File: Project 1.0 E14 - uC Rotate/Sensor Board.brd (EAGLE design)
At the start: 40 x 75 mm, 95 parts, among them IC1 LT1963EST-1.5, IC2 LT1963EST-1.5, IC4 LT1963EST-1.5

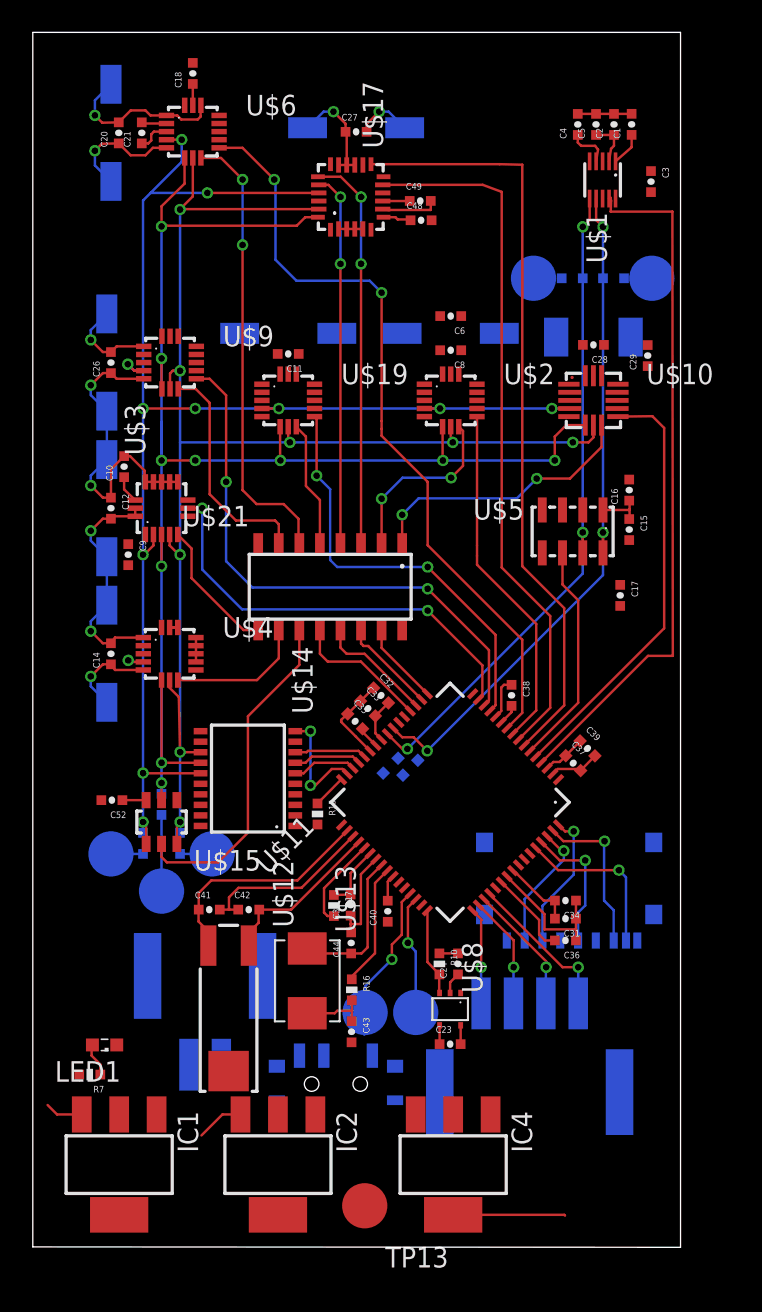
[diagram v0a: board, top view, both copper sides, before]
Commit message: Sensor test board: All traces have been confirmed connected except for power and GND. The issues from previous commit remain to be addresed.
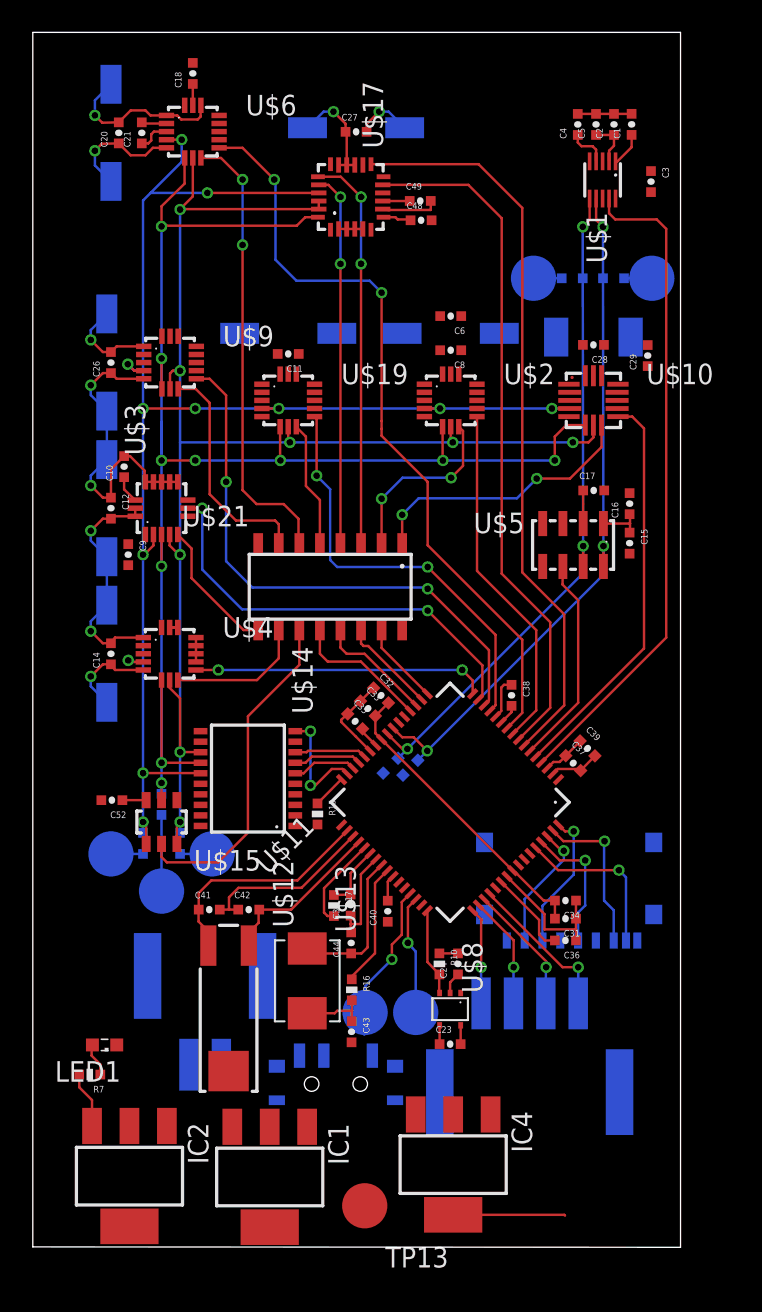
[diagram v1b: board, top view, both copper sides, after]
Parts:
- moved IC1 9.33 mm to (14.6, 4.32)
- moved IC2 9.20 mm to (5.97, 4.37)
- moved C17 6.68 mm to (34.6, 46.7), turned to 0 degrees
- moved C15 0.84 mm to (36.9, 43.5)
- moved C16 0.84 mm to (36.9, 45.9)
- moved U$5 0.84 mm to (33.4, 43.3)
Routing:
- net INT2-LPS331: track 0.00 -> 18.2 mm, vias 0 -> 2
- net 1.2V: track 7.31 -> 18.8 mm
- net 3.0V: track 2.35 -> 0.00 mm
- net INT1-MAG3110: track 43.1 -> 41.0 mm
- net N$5: track 0.00 -> 2.04 mm
- net INT2-ADXL362: track 26.7 -> 25.0 mm
- net N$26: track 0.00 -> 1.74 mm
- net N$24: track 0.00 -> 1.72 mm
- net LSM9D-INT1-XM: track 47.3 -> 45.7 mm
- net MISO-B: track 89.4 -> 90.8 mm
- net LSM9D-INT-G: track 43.3 -> 42.4 mm
- net INT1-MPL311: track 13.9 -> 13.0 mm
- net SDA-0: track 41.5 -> 42.4 mm
- net SCL-0: track 42.7 -> 43.6 mm
- net MOSI-B: track 96.0 -> 96.7 mm

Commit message: Sensor Test Board: Corrected LSM9D0 interrupt issue by adding int2-XM and removing int1_G and replacing it with DRDY_G. Some 3.3v traces have been connected but these wil need to be checked to ensure the LDO is not overloaded.
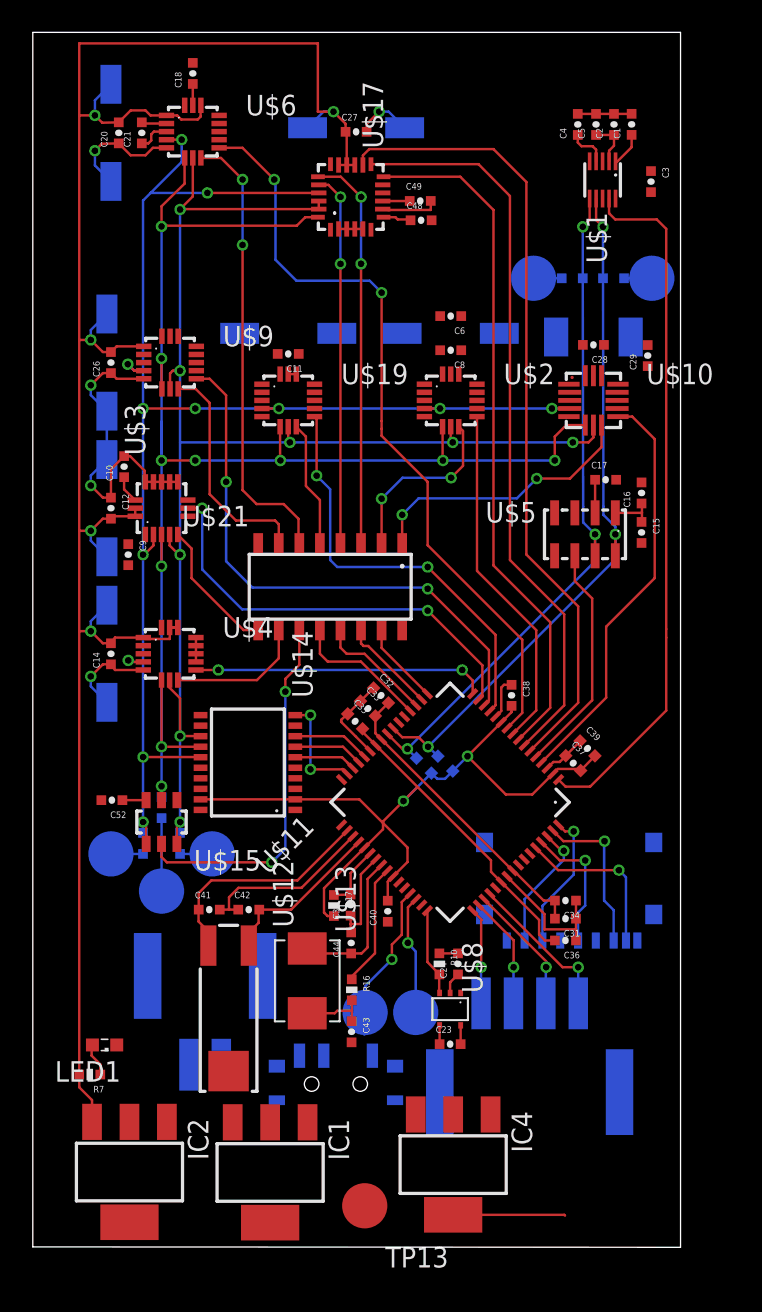
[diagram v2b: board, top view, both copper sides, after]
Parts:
- removed R15: 1M, Kas-Passives:0402-RES
- moved R1 2.17 mm to (25.5, 29.8), turned to 225 degrees
- moved R2 2.06 mm to (24.2, 29.7), turned to 225 degrees
- moved U$14 0.99 mm to (13.3, 29.9)
- moved C17 0.99 mm to (35.4, 47.4)
- moved C16 0.99 mm to (37.6, 46.6)
- moved U$5 0.99 mm to (34.1, 44.0)
- moved C15 0.99 mm to (37.6, 44.1)
- moved IC1 0.28 mm to (14.7, 4.60)
- moved IC2 0.25 mm to (5.97, 4.62)
- moved R4 0.20 mm to (7.95, 27.1)
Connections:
- removed net N$18: R15.1, U$11.P$32
- new net LSM9D-INT2-XM: U$11.P$6, U$17.P$14
- net 3.3V: no longer R15.2
- net INT1-MAG3110: now also U$11.P$1; no longer U$11.P$4
- net INT1-MPL311: now also U$11.P$5; no longer U$11.P$6
- net INT2-ADXL362: now also U$11.P$4; no longer U$11.P$5
- net LSM9D-DRGY-G: now also U$11.P$8
- net LSM9D-INT-G: no longer U$11.P$8
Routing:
- net 3.3V: track 64.1 -> 198.4 mm, vias 5 -> 7
- net LSM9D-INT2-XM: track 0.00 -> 49.4 mm
- net LSM9D-DRGY-G: track 0.00 -> 42.6 mm
- net LSM9D-INT-G: track 42.4 -> 0.00 mm
- net INT1-MAG3110: track 41.0 -> 43.4 mm
- net N$18: track 2.10 -> 0.00 mm
- net CS-ADT7301: track 20.9 -> 22.8 mm, vias 0 -> 2
- net INT1-MPL311: track 13.0 -> 14.3 mm
- net MISO-B: track 90.8 -> 89.8 mm
- net MOSI-B: track 96.7 -> 95.7 mm
- net INT2-ADXL362: track 25.0 -> 25.7 mm
- net SDA-0: track 42.4 -> 43.0 mm

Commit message: Sensor Test Board: Added library component (Atmel Tem sensor) and named one net so that it reflected its function and connected as needed (3.3V)
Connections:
- removed net LSM9D-INT-G: U$17.P$11
- removed net N$25: C15.1, C16.1, U$5.P$1
- net 3.3V: now also C15.1, C16.1, U$5.P$1
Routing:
- net N$25: track 2.83 -> 0.00 mm
- net 3.3V: track 198.4 -> 201.2 mm
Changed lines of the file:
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@@
 <wire x1="8.4582" y1="37.5412" x2="8.4582" y2="38.2518" width="0.1524" layer="1"/>
 <wire x1="8.4582" y1="38.2518" x2="8.4502875" y2="38.2518" width="0.1524" layer="1"/>
+<contactref element="U$5" pad="P$1"/>
+<contactref element="C15" pad="1"/>
+<contactref element="C16" pad="1"/>
+<wire x1="37.592" y1="45.9082" x2="37.6174" y2="45.9082" width="0.1524" layer="1"/>
+<wire x1="37.6174" y1="45.9082" x2="37.6174" y2="45.3296" width="0.1524" layer="1"/>
+<wire x1="37.6174" y1="45.3296" x2="37.6174" y2="44.7698" width="0.1524" layer="1"/>
+<wire x1="37.592" y1="44.7698" x2="37.6174" y2="44.7698" width="0.1524" layer="1"/>
+<wire x1="35.9738" y1="45.3296" x2="37.6174" y2="45.3296" width="0.1524" layer="1"/>
 <wire x1="35.5868" y1="67.0376" x2="38.1762" y2="66.436" width="0" layer="19" extent="1-1"/>
 <wire x1="35.1868" y1="64.7376" x2="35.5868" y2="67.0376" width="0" layer="19" extent="1-1"/>
@@
 <wire x1="5.8928" y1="43.3982" x2="6.9502" y2="43.9934" width="0" layer="19" extent="1-1"/>
 <wire x1="32.2238" y1="45.3296" x2="33.1072" y2="53.2732" width="0" layer="19" extent="1-1"/>
+<wire x1="35.9738" y1="45.3296" x2="32.2238" y2="45.3296" width="0" layer="19" extent="1-1"/>
 <wire x1="10.3592" y1="27.63755" x2="8.4582" y2="37.5412" width="0" layer="19" extent="1-1"/>
 <wire x1="22.9108" y1="27.560409375" x2="22.89024375" y2="27.5336" width="0" layer="19" extent="1-16"/>
@@
 <contactref element="U$16" pad="P$2"/>
 <wire x1="11.6426" y1="11.2502" x2="17.9698" y2="11.8084" width="0" layer="19" extent="16-16"/>
-</signal>
-<signal name="N$25">
-<contactref element="U$5" pad="P$1"/>
-<contactref element="C15" pad="1"/>
-<contactref element="C16" pad="1"/>
-<wire x1="37.592" y1="45.9082" x2="37.6174" y2="45.9082" width="0.1524" layer="1"/>
-<wire x1="37.6174" y1="45.9082" x2="37.6174" y2="45.3296" width="0.1524" layer="1"/>
-<wire x1="37.6174" y1="45.3296" x2="37.6174" y2="44.7698" width="0.1524" layer="1"/>
-<wire x1="37.592" y1="44.7698" x2="37.6174" y2="44.7698" width="0.1524" layer="1"/>
-<wire x1="35.9738" y1="45.3296" x2="37.6174" y2="45.3296" width="0.1524" layer="1"/>
 </signal>
 <signal name="SCLK-B">
@@
 <contactref element="U$17" pad="P$10"/>
 </signal>
-<signal name="LSM9D-INT-G">
-<contactref element="U$17" pad="P$11"/>
-</signal>
 <signal name="LSM9D-DRGY-G">

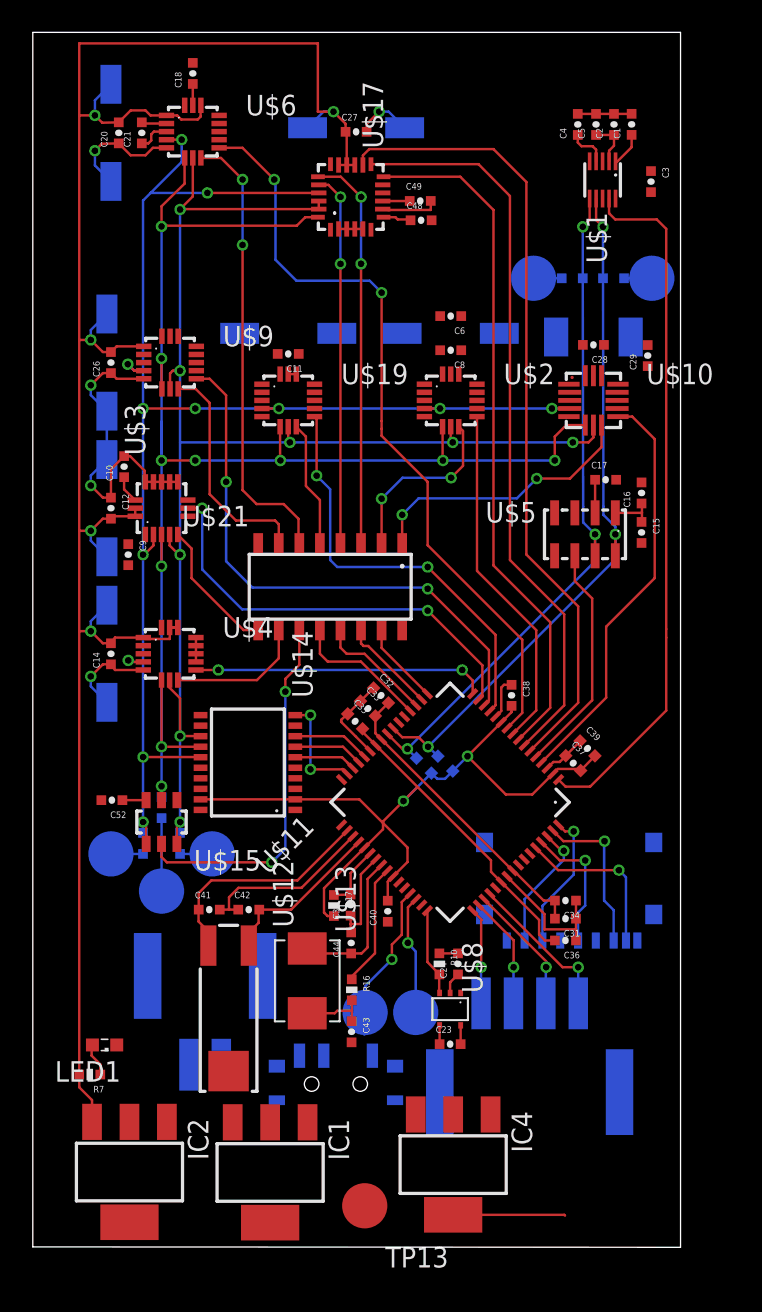
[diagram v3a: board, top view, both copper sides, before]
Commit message: Sensor Test Board: Added humidity sensor to the I2C lines. Changed packages from hand solder to oven, and corrected small missalignment in some packages. Two humidity sensors and one crystal were added to the libraries
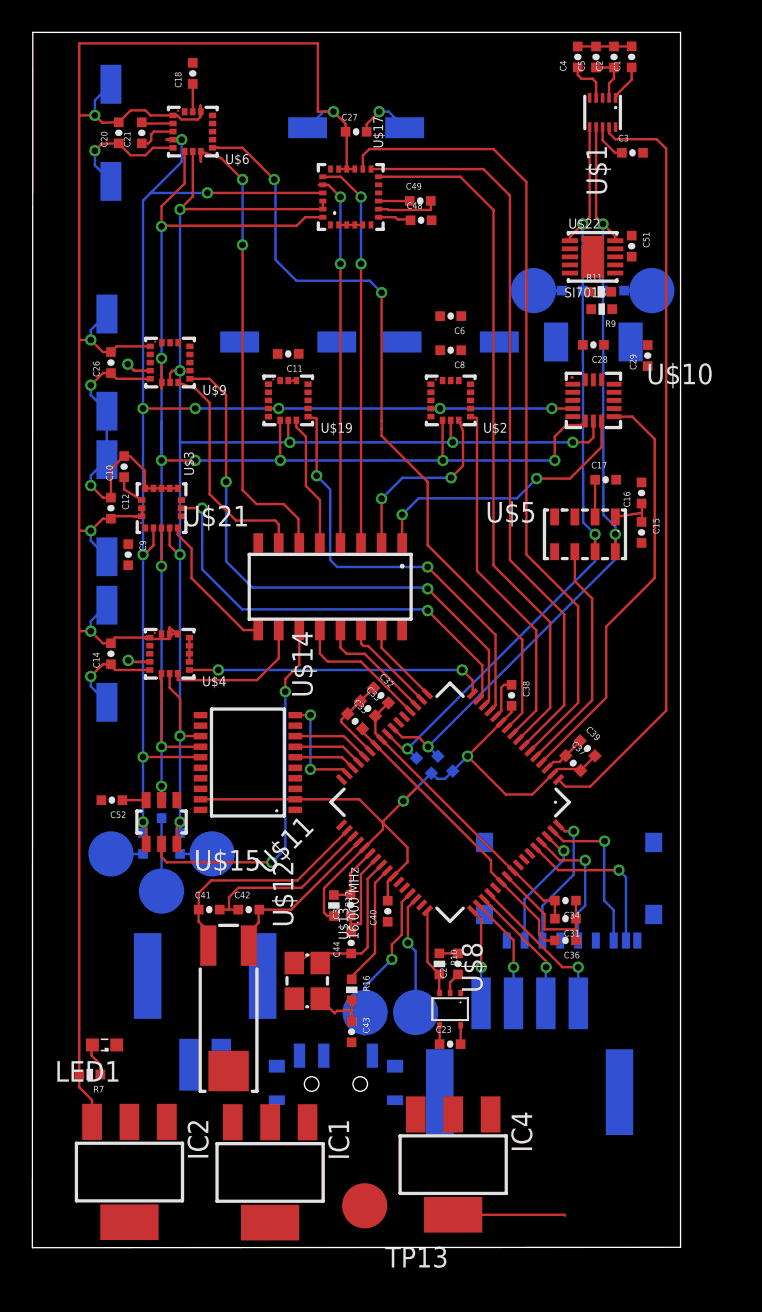
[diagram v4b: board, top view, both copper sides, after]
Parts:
- added C51: (no value), Kas-Passives:C0402
- added R11: 1.0k, Kas-Passives:0402-RES
- added R9: 2.0k, Kas-Passives:0402-RES
- added U$22: SI7013, Kas-Sensors:DFN-10(3X3)
- C1, C10, C11, C12, C14, C15, C16, C17, C18, C2, C20, C21, C23, C24, C26, C27, C28, C29, C3, C30, C31, C32, C33, C34, C35, C36, C37, C38, C39, C4, C40, C41, C42, C43, C44, C48, C49, C5, C52, C6, C8, C9: device Kas-Passives:0402-CAP -> Kas-Passives:C0402
- U$1: value MAG3110_HS -> MAG3110; device Kas-Sensors:DFN-10(2X2)_HS -> Kas-Sensors:DFN-10(2X2)
- U$10: device Kas-Sensors:LGA-16(3X3.25)_HS -> Kas-Sensors:LGA-16(3X3.25)
- U$13: device Kas-Crystal:2-SMD -> Kas-Crystal:4-SMD(3.2X2.5)
- U$17: value LSM9DS0_HS -> LSM9DS0; device Kas-Sensors:LGA-24(4X4)_HS -> Kas-Sensors:LGA-24(4X4)
- U$19: value MAX21000_HS -> MAX21000; device Kas-Sensors:LGA-16(3X3)_HS -> Kas-Sensors:LGA-16(3X3)
- U$2: value H3LIS331DLTR_HS -> H3LIS331DLTR; device Kas-Sensors:LGA-16(3X3)_HS -> Kas-Sensors:LGA-16(3X3)
- U$3: value L3GD20H_HS -> L3GD20H; device Kas-Sensors:LGA-16(3X3)_HS -> Kas-Sensors:LGA-16(3X3)
- U$4: value LPS331AP_HS -> LPS331AP; device Kas-Sensors:LGA-16(3X3)_HS -> Kas-Sensors:LGA-16(3X3)
- U$5: value MPL3115A2_HS -> MPL3115A2; device Kas-Sensors:LGA-8(5X3)_HS -> Kas-Sensors:LGA-8(5X3)
- U$6: value LSM303D_HS -> LSM303D; device Kas-Sensors:LGA-16(3X3)_HS -> Kas-Sensors:LGA-16(3X3)
- U$9: device Kas-Sensors:LGA-16(3X3)_HS -> Kas-Sensors:LGA-16(3X3)
- moved C2 4.17 mm to (35.9, 73.5)
- moved C4 4.17 mm to (33.7, 73.5)
- moved C5 4.17 mm to (34.8, 73.5)
- moved C1 4.17 mm to (37.0, 73.5)
- moved U$1 4.17 mm to (35.2, 70.1)
- moved C3 2.11 mm to (37.0, 67.6), turned to 0 degrees
- moved R5 0.76 mm to (35.9, 59.1)
- moved R8 0.76 mm to (33.3, 59.1)
- moved TP5 0.76 mm to (30.9, 59.1)
- moved TP6 0.76 mm to (38.2, 59.1)
- moved C54 0.53 mm to (15.8, 55.9)
- moved C7 0.53 mm to (25.8, 55.9)
- moved C19 0.30 mm to (34.6, 55.9)
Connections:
- new net N$18: R11.2, R9.1, U$22.P$6
- net 3.0V: now also R9.2
- net 3.3V: now also C51.2, U$22.P$8, U$22.P$9
- net GND: now also C51.1, R11.1, U$22.P$2, U$22.P$3, U$22.P$4, U$22.P$7
- net N$16: now also U$13.P$3; no longer U$13.P$2
- net SCL-0: now also U$22.P$10
- net SDA-0: now also U$22.P$1
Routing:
- net SDA-0: track 43.0 -> 48.5 mm
- net SCL-0: track 43.9 -> 49.4 mm
- net 3.3V: track 201.2 -> 206.7 mm
- net INT1-MAG3110: track 43.4 -> 47.8 mm
- net MOSI-B: track 95.7 -> 98.4 mm
- net MISO-B: track 89.8 -> 91.9 mm
- net SCLK-B: track 94.2 -> 95.9 mm
- net GND: track 77.7 -> 79.3 mm
- net CS-LSM303: track 28.5 -> 29.8 mm
- net N$16: track 9.47 -> 10.3 mm
- net INT2-LSM303: track 47.5 -> 48.3 mm
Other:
- board size 40 x 75 mm -> 40 x 75.1 mm
